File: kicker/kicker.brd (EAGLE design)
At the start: 59.7 x 56.3 mm, 23 parts, among them T1 NPN_BC817,215, T3 NPN_BC817,215, X1 JST-XH-06-PIN-LONG-PAD

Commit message: Updating designs
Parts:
- added T2, T4: NPN_BC817,215, rhoban:SOT-23
- R1, R4: value 1K -> 3K
- moved R32 5.55 mm to (51.8, 20.8)
- moved R2 5.39 mm to (44.5, 20.8)
- moved R4 4.58 mm to (51.8, 13.7)
- moved R1 4.19 mm to (44.2, 14.0), turned to 0 degrees
- moved R33 3.18 mm to (55.4, 24.4)
- moved T3 3.18 mm to (51.8, 24.4)
- moved R3 2.90 mm to (48.0, 24.4)
- moved T1 2.90 mm to (44.5, 24.4)
- moved R34 1.70 mm to (46.2, 8.89)
- moved R35 1.52 mm to (51.1, 8.89)
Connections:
- new net N$5: R1.1, T2.1
- new net N$6: R4.1, T4.1
- net GND: now also T2.2, T4.2
- net KICK1: now also R1.2; no longer R1.1
- net N$1: now also T2.3; no longer R1.2
- net N$3: now also T4.3; no longer R4.1
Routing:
- net CAP: track 10.0 -> 8.67 mm

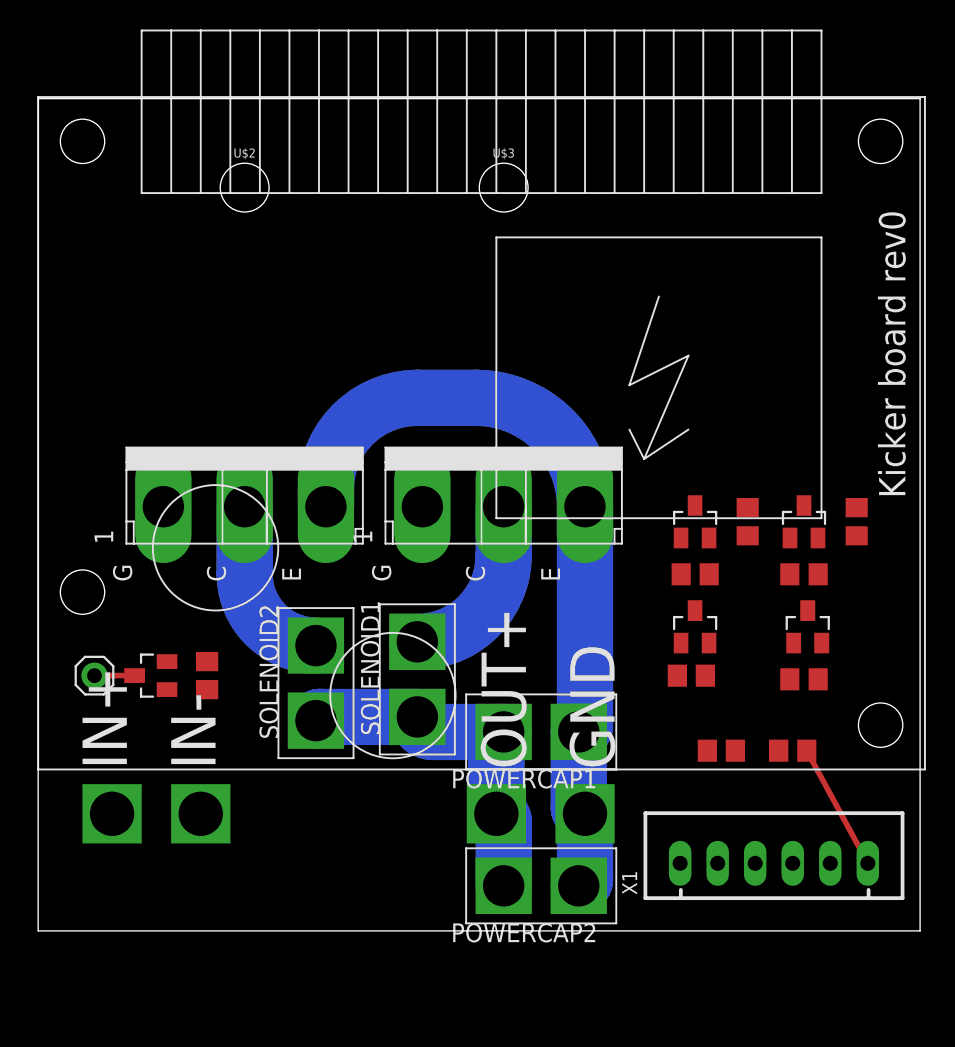
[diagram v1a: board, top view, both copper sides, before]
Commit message: Adding resistor on big mos gates
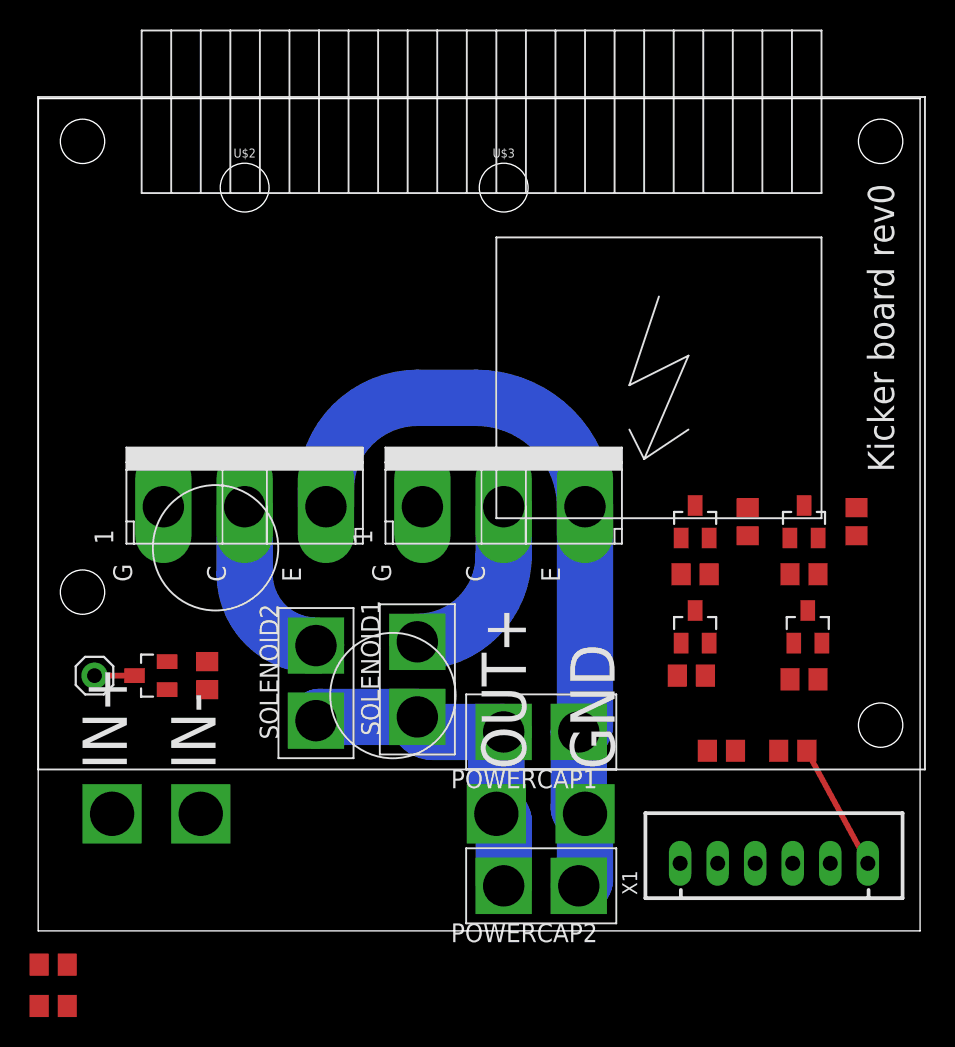
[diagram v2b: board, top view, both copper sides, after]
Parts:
- added R5, R6: 1K, rhoban:R0805
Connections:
- new net N$7: R5.1, U$1.P$1
- new net N$8: R6.1, U$11.P$1
- net N$35: now also R6.2; no longer U$11.P$1
- net N$4: now also R5.2; no longer U$1.P$1
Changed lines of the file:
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@@
 <wire x1="18.796" y1="16.002" x2="13.97" y2="20.828" width="3.81" layer="30" curve="-90"/>
 <wire x1="13.97" y1="20.828" x2="13.97" y2="25.4" width="3.81" layer="30"/>
-<text x="56.896" y="45.466" size="1.778" layer="25" rot="R270">Kicker board rev0</text>
+<text x="56.134" y="47.244" size="1.778" layer="25" rot="R270">Kicker board rev0</text>
 <wire x1="19.304" y1="25.4" x2="19.304" y2="26.162" width="3.81" layer="30"/>
 <wire x1="19.304" y1="26.162" x2="25.908" y2="32.766" width="3.81" layer="30" curve="-90"/>
@@
 <attribute name="FARNELL" value="2446965" x="51.816" y="13.716" size="1.778" layer="27" display="off"/>
 </element>
+<element name="R5" library="rhoban" package="R0805" value="1K" x="1.016" y="-5.588">
+<attribute name="FARNELL" value="2446965" x="1.016" y="-5.588" size="1.778" layer="27" display="off"/>
+</element>
+<element name="R6" library="rhoban" package="R0805" value="1K" x="1.016" y="-8.382">
+<attribute name="FARNELL" value="2446965" x="1.016" y="-8.382" size="1.778" layer="27" display="off"/>
+</element>
 </elements>
 <signals>
@@
 <contactref element="T1" pad="3"/>
 <contactref element="R3" pad="1"/>
-<contactref element="U$1" pad="P$1"/>
-<wire x1="44.45" y1="25.484" x2="48.006" y2="25.334" width="0" layer="19" extent="1-1"/>
-<wire x1="25.996" y1="25.4" x2="44.45" y2="25.484" width="0" layer="19" extent="1-1"/>
+<contactref element="R5" pad="2"/>
+<wire x1="48.006" y1="25.334" x2="44.45" y2="25.484" width="0" layer="19" extent="1-1"/>
+<wire x1="1.966" y1="-5.588" x2="44.45" y2="25.484" width="0" layer="19" extent="1-1"/>
 </signal>
 <signal name="VIN" class="2">
@@
 <contactref element="T3" pad="3"/>
 <contactref element="R33" pad="1"/>
-<contactref element="U$11" pad="P$1"/>
-<wire x1="51.816" y1="25.484" x2="55.372" y2="25.334" width="0" layer="19" extent="1-1"/>
-<wire x1="8.47" y1="25.4" x2="51.816" y2="25.484" width="0" layer="19" extent="1-1"/>
+<contactref element="R6" pad="2"/>
+<wire x1="55.372" y1="25.334" x2="51.816" y2="25.484" width="0" layer="19" extent="1-1"/>
+<wire x1="1.966" y1="-8.382" x2="51.816" y2="25.484" width="0" layer="19" extent="1-1"/>
 </signal>
 <signal name="N$36" class="2">
@@
 <wire x1="52.07" y1="18.372" x2="50.866" y2="20.828" width="0" layer="19" extent="1-1"/>
 </signal>
+<signal name="N$7">
+<contactref element="U$1" pad="P$1"/>
+<contactref element="R5" pad="1"/>
+<wire x1="0.066" y1="-5.588" x2="25.996" y2="25.4" width="0" layer="19" extent="1-1"/>
+</signal>
+<signal name="N$8">
+<contactref element="R6" pad="1"/>
+<contactref element="U$11" pad="P$1"/>
+<wire x1="0.066" y1="-8.382" x2="8.47" y2="25.4" width="0" layer="19" extent="1-1"/>
+</signal>
 </signals>

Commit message: 1K on grid
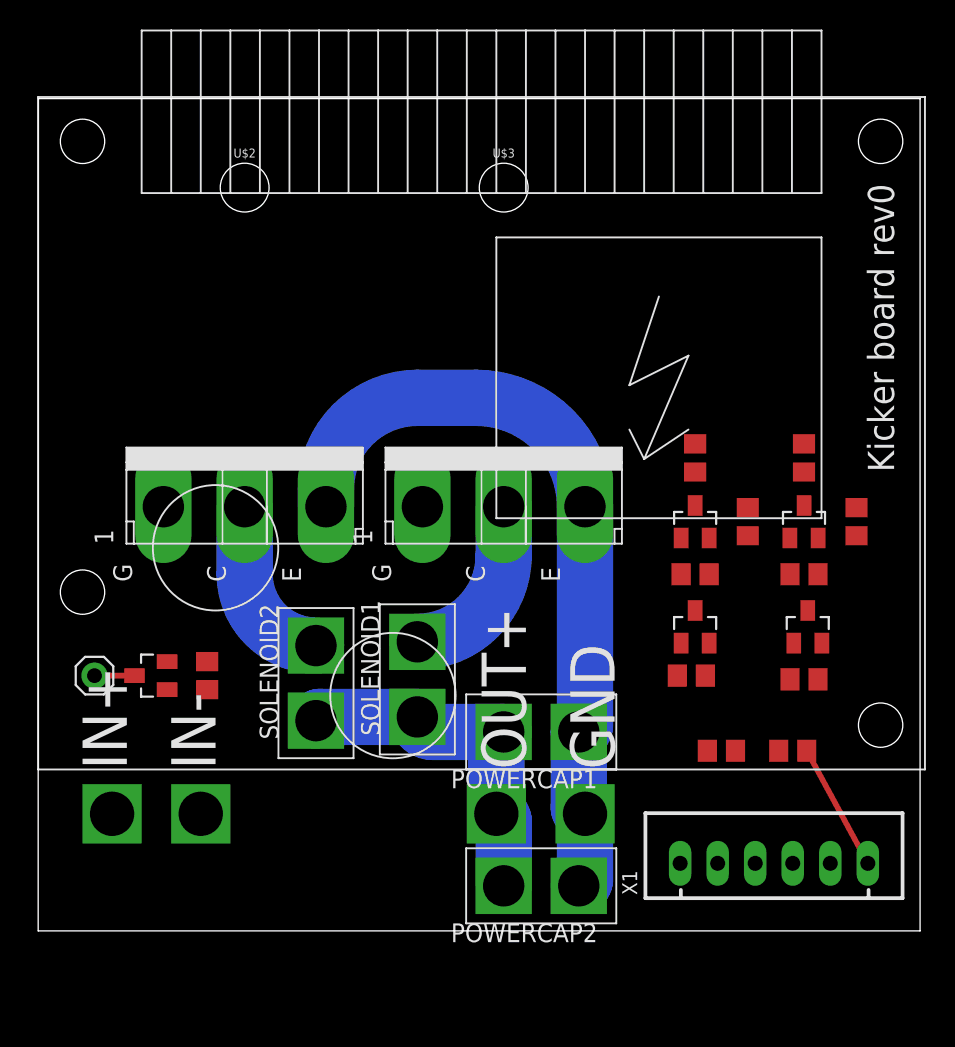
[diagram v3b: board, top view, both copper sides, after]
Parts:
- moved R6 62.9 mm to (51.8, 28.7), turned to 270 degrees
- moved R5 55.3 mm to (44.5, 28.7), turned to 270 degrees
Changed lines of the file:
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@@
 <setting verticaltext="up"/>
 </settings>
-<grid distance="0.01" unitdist="inch" unit="inch" style="lines" multiple="1" display="no" altdistance="0.025" altunitdist="inch" altunit="inch"/>
+<grid distance="0.254" unitdist="mm" unit="mm" style="lines" multiple="1" display="no" altdistance="0.025" altunitdist="inch" altunit="inch"/>
 <layers>
 <layer number="1" name="Top" color="4" fill="1" visible="yes" active="yes"/>
@@
 <attribute name="FARNELL" value="2446965" x="51.816" y="13.716" size="1.778" layer="27" display="off"/>
 </element>
-<element name="R5" library="rhoban" package="R0805" value="1K" x="1.016" y="-5.588">
-<attribute name="FARNELL" value="2446965" x="1.016" y="-5.588" size="1.778" layer="27" display="off"/>
-</element>
-<element name="R6" library="rhoban" package="R0805" value="1K" x="1.016" y="-8.382">
-<attribute name="FARNELL" value="2446965" x="1.016" y="-8.382" size="1.778" layer="27" display="off"/>
+<element name="R5" library="rhoban" package="R0805" value="1K" x="44.45" y="28.702" rot="R270">
+<attribute name="FARNELL" value="2446965" x="44.45" y="28.702" size="1.778" layer="27" rot="R270" display="off"/>
+</element>
+<element name="R6" library="rhoban" package="R0805" value="1K" x="51.816" y="28.702" rot="R270">
+<attribute name="FARNELL" value="2446965" x="51.816" y="28.702" size="1.778" layer="27" rot="R270" display="off"/>
 </element>
 </elements>
@@
 <contactref element="X1" pad="5"/>
 <contactref element="R4" pad="2"/>
-<wire x1="52.766" y1="13.716" x2="53.594" y2="1.27" width="0" layer="19" extent="1-1"/>
+<wire x1="53.594" y1="1.27" x2="52.766" y2="13.716" width="0" layer="19" extent="1-1"/>
 </signal>
 <signal name="GND" class="2">
@@
 <contactref element="T2" pad="2"/>
 <contactref element="T4" pad="2"/>
+<wire x1="53.02" y1="16.172" x2="52.766" y2="23.284" width="0" layer="19" extent="1-1"/>
 <wire x1="45.4" y1="23.284" x2="52.766" y2="23.284" width="0" layer="19" extent="1-1"/>
+<wire x1="45.4" y1="16.172" x2="45.4" y2="23.284" width="0" layer="19" extent="1-1"/>
+<wire x1="50.104" y1="8.89" x2="53.02" y2="16.172" width="0" layer="19" extent="1-1"/>
 <wire x1="36.996" y1="25.4" x2="45.4" y2="23.284" width="0" layer="19" extent="1-1"/>
 <wire x1="43.434" y1="1.27" x2="37" y2="0.17" width="0" layer="19" extent="16-16"/>
-<wire x1="50.104" y1="8.89" x2="45.4" y2="23.284" width="0" layer="19" extent="1-1"/>
 <wire x1="8.72" y1="14.92" x2="19.47" y2="25.4" width="0" layer="19" extent="1-1"/>
 <wire x1="11" y1="4.62" x2="8.72" y2="14.92" width="0" layer="19" extent="1-1"/>
-<wire x1="45.4" y1="16.172" x2="11" y2="4.62" width="0" layer="19" extent="1-1"/>
-<wire x1="53.02" y1="16.172" x2="45.4" y2="16.172" width="0" layer="19" extent="1-1"/>
 </signal>
 <signal name="N$4">
@@
 <contactref element="R3" pad="1"/>
 <contactref element="R5" pad="2"/>
+<wire x1="44.45" y1="27.752" x2="44.45" y2="25.484" width="0" layer="19" extent="1-1"/>
 <wire x1="48.006" y1="25.334" x2="44.45" y2="25.484" width="0" layer="19" extent="1-1"/>
-<wire x1="1.966" y1="-5.588" x2="44.45" y2="25.484" width="0" layer="19" extent="1-1"/>
 </signal>
 <signal name="VIN" class="2">
@@
 <contactref element="R33" pad="1"/>
 <contactref element="R6" pad="2"/>
+<wire x1="51.816" y1="27.752" x2="51.816" y2="25.484" width="0" layer="19" extent="1-1"/>
 <wire x1="55.372" y1="25.334" x2="51.816" y2="25.484" width="0" layer="19" extent="1-1"/>
-<wire x1="1.966" y1="-8.382" x2="51.816" y2="25.484" width="0" layer="19" extent="1-1"/>
 </signal>
 <signal name="N$36" class="2">
@@
 <contactref element="R35" pad="2"/>
 <contactref element="X1" pad="6"/>
+<wire x1="56.134" y1="1.27" x2="52.004" y2="8.89" width="0.381" layer="1"/>
 <wire x1="47.178" y1="8.89" x2="52.004" y2="8.89" width="0" layer="19" extent="1-1"/>
-<wire x1="56.134" y1="1.27" x2="52.004" y2="8.89" width="0.381" layer="1"/>
 </signal>
 <signal name="BOOST_EN">
@@
 <contactref element="T2" pad="1"/>
 <contactref element="R1" pad="1"/>
-<wire x1="43.5" y1="16.172" x2="43.246" y2="13.97" width="0" layer="19" extent="1-1"/>
+<wire x1="43.246" y1="13.97" x2="43.5" y2="16.172" width="0" layer="19" extent="1-1"/>
 </signal>
 <signal name="N$6">
 <contactref element="T4" pad="1"/>
 <contactref element="R4" pad="1"/>
-<wire x1="51.12" y1="16.172" x2="50.866" y2="13.716" width="0" layer="19" extent="1-1"/>
+<wire x1="50.866" y1="13.716" x2="51.12" y2="16.172" width="0" layer="19" extent="1-1"/>
 </signal>
 <signal name="N$3">
@@
 <contactref element="U$1" pad="P$1"/>
 <contactref element="R5" pad="1"/>
-<wire x1="0.066" y1="-5.588" x2="25.996" y2="25.4" width="0" layer="19" extent="1-1"/>
+<wire x1="25.996" y1="25.4" x2="44.45" y2="29.652" width="0" layer="19" extent="1-1"/>
 </signal>
 <signal name="N$8">
 <contactref element="R6" pad="1"/>
 <contactref element="U$11" pad="P$1"/>
-<wire x1="0.066" y1="-8.382" x2="8.47" y2="25.4" width="0" layer="19" extent="1-1"/>
+<wire x1="8.47" y1="25.4" x2="51.816" y2="29.652" width="0" layer="19" extent="1-1"/>
 </signal>
 </signals>
